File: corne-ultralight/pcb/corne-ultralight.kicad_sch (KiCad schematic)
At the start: 108 parts, among them J2 OLED, J7 OLED, SW1 SW_PUSH, SW10 SW_PUSH, SW11 SW_PUSH, SW12 SW_PUSH, SW13 SW_PUSH, SW14 SW_PUSH, SW15 SW_PUSH, SW16 SW_PUSH, SW17 SW_PUSH, SW18 SW_PUSH, SW19 SW_PUSH, SW2 SW_PUSH, SW20 SW_PUSH, SW21 SW_PUSH, SW22 SW_PUSH, SW23 SW_PUSH, SW24 SW_PUSH, SW25 SW_PUSH, SW26 SW_PUSH, SW27 SW_PUSH, SW28 SW_PUSH, SW29 SW_PUSH, SW3 SW_PUSH, SW30 SW_PUSH, SW31 SW_PUSH, SW32 SW_PUSH, SW33 SW_PUSH, SW34 SW_PUSH, SW35 SW_PUSH, SW36 SW_PUSH, SW37 SW_PUSH, SW38 SW_PUSH, SW39 SW_PUSH, SW4 SW_PUSH, SW40 SW_PUSH, SW41 SW_PUSH, SW42 SW_PUSH, SW5 SW_PUSH, SW6 SW_PUSH, SW7 SW_PUSH, SW8 SW_PUSH, SW9 SW_PUSH, U1 ProMicro, U2 ProMicro

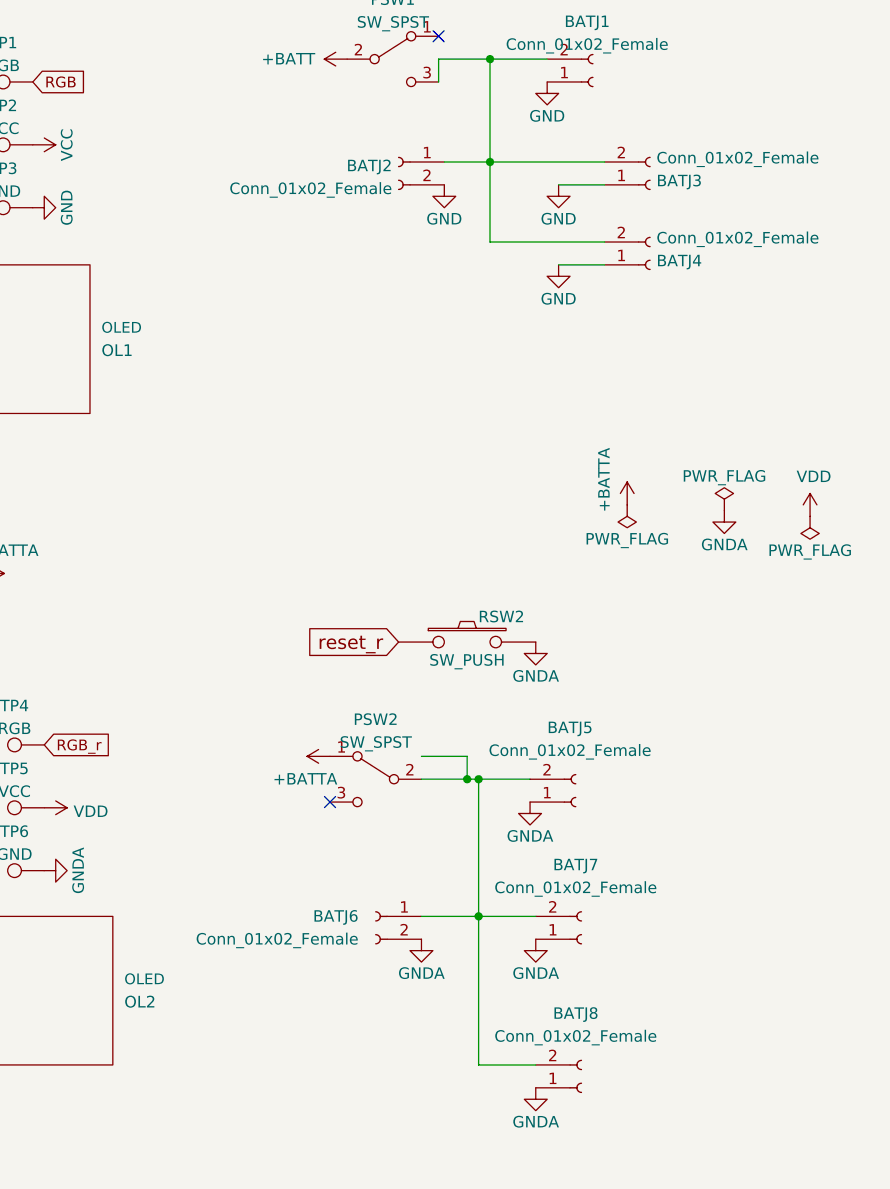
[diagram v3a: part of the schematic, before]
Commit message: Bottom JST connectors aligned
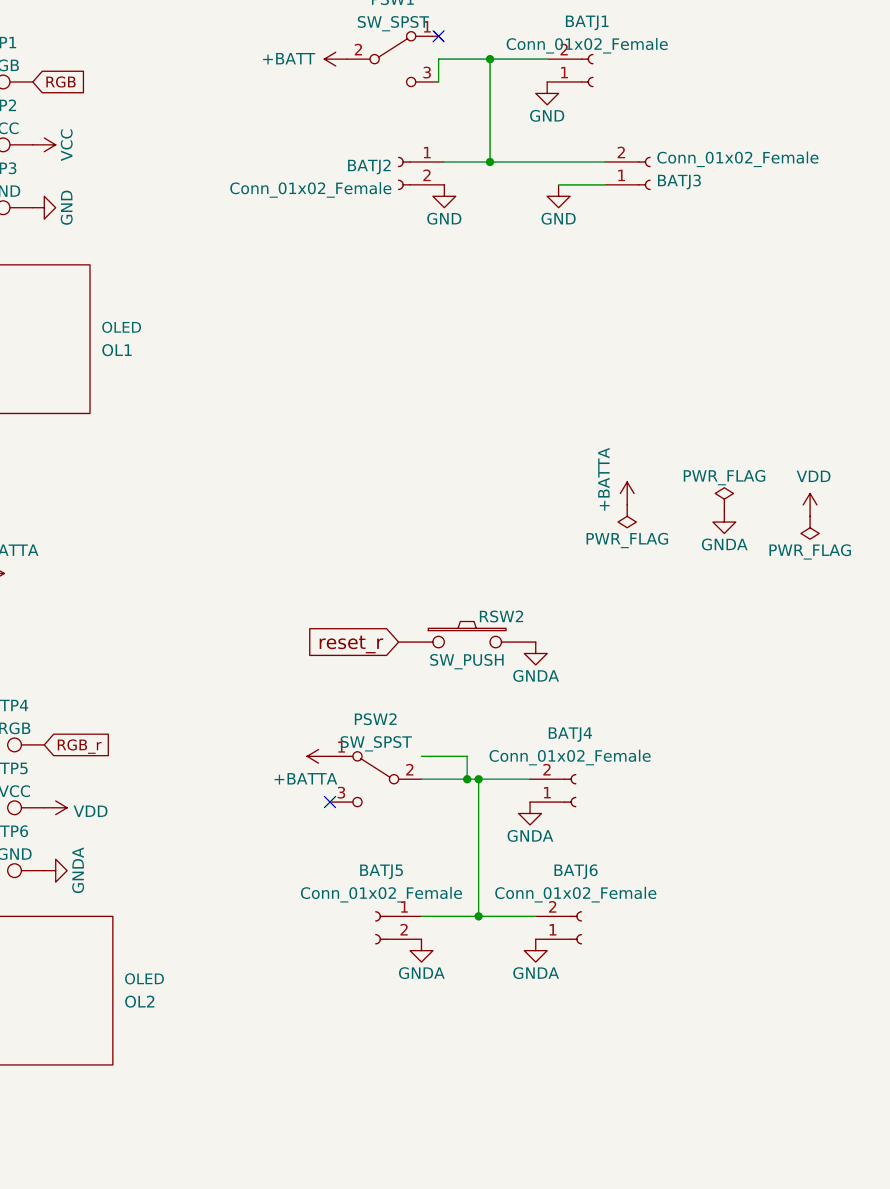
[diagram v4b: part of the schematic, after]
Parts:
- removed BATJ4, BATJ8: Conn_01x02_Female, Connector_JST:JST_PH_S2B-PH-K_1x02_P2.00mm_Horizontal, symbol Connector:Conn_01x02_Female
- renumbered BATJ5 to BATJ4, BATJ6 to BATJ5, BATJ7 to BATJ6

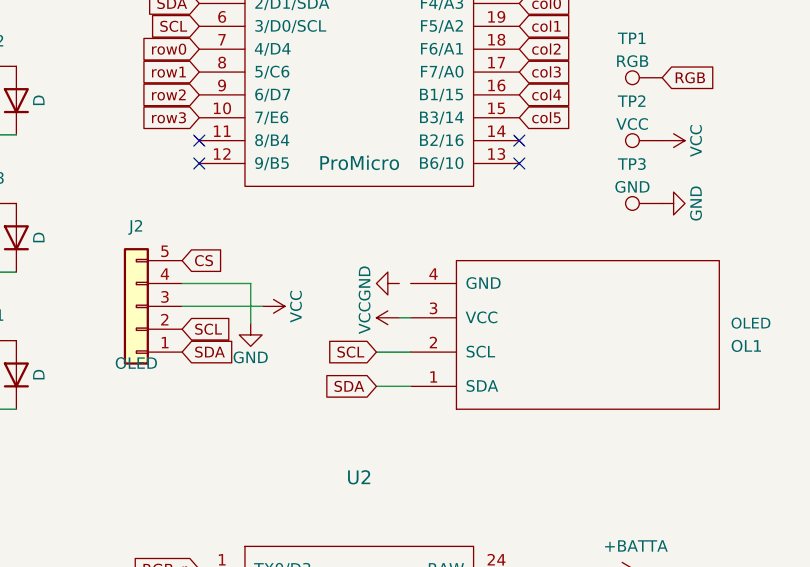
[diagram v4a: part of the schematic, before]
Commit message: All JST connectors routed
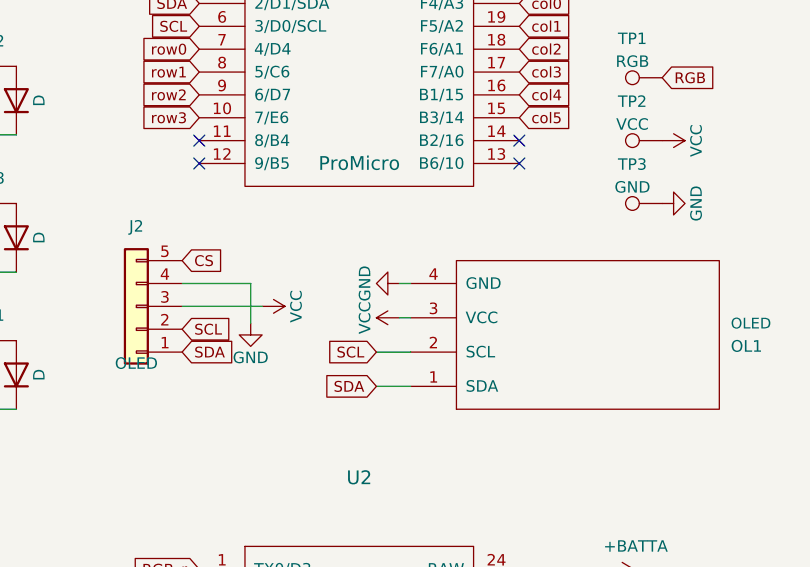
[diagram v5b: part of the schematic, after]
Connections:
- net GND: now also OL1.4 (GND)
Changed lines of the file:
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@@
+	(wire
+		(pts
+			(xy 162.56 63.5) (xy 163.83 63.5)
+		)
+		(stroke
+			(width 0)
+			(type default)
+		)
+	)
 	(wire
 		(pts

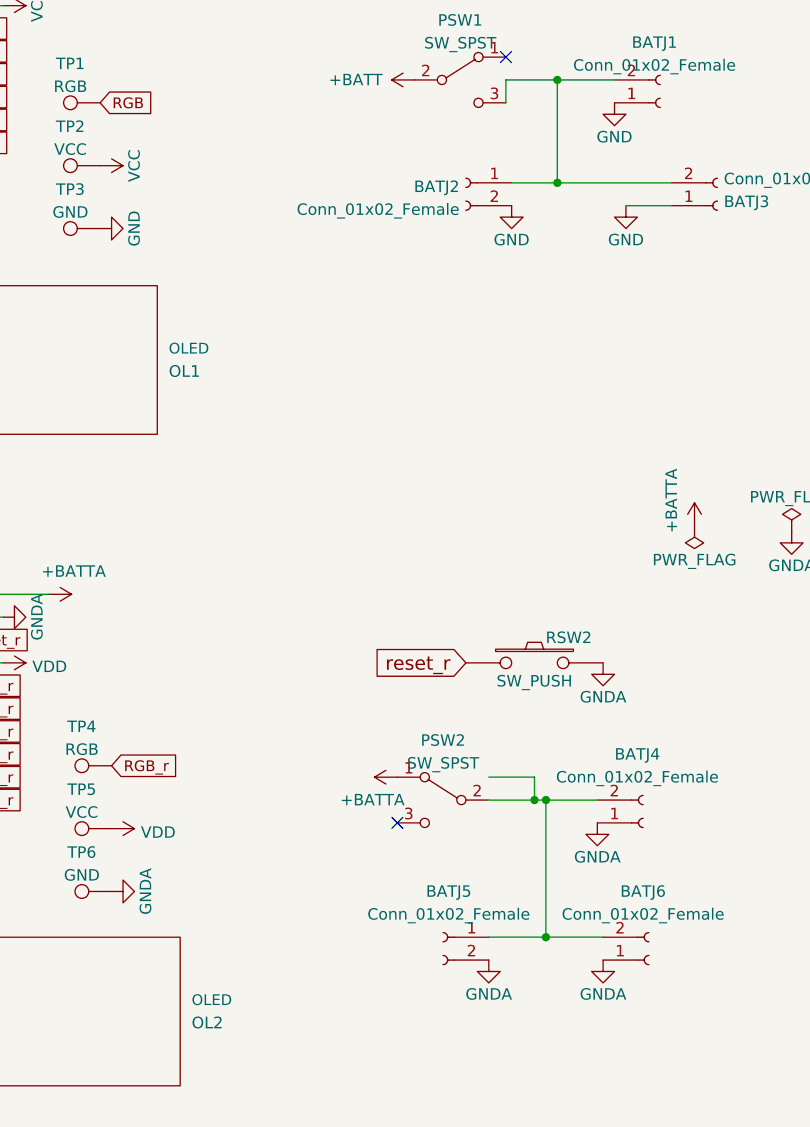
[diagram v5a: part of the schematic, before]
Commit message: BAT pines assignment fixes
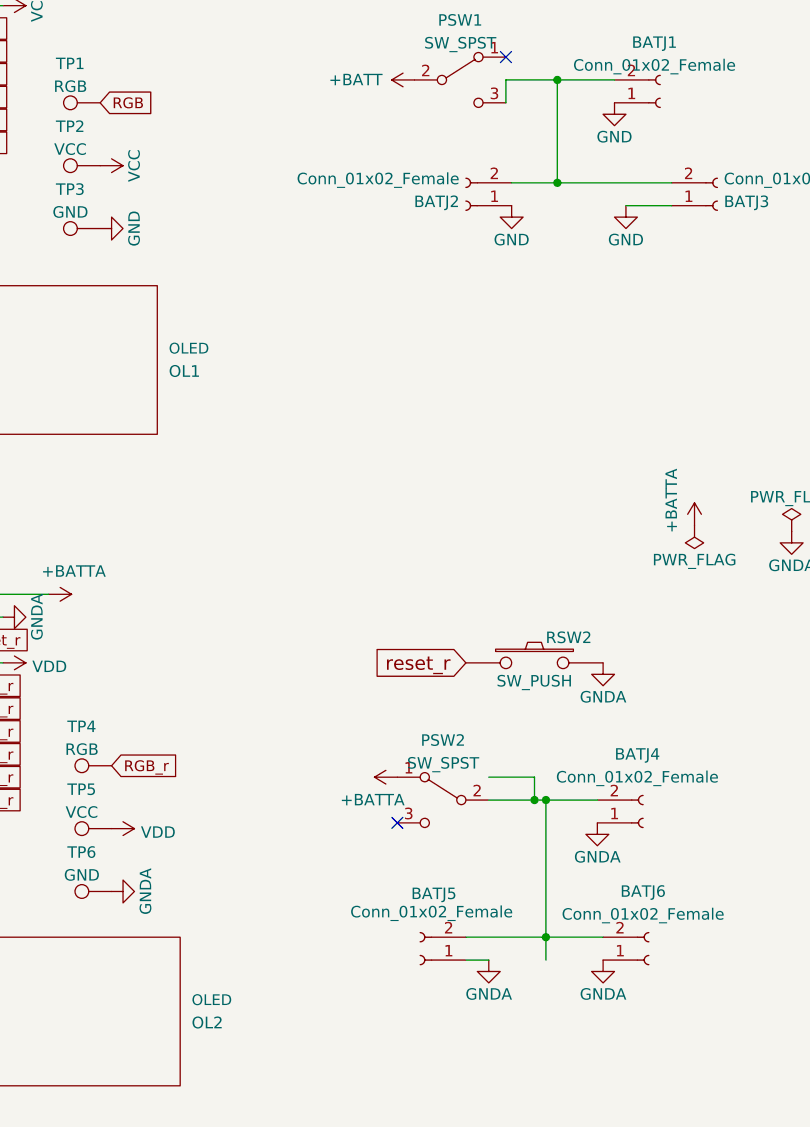
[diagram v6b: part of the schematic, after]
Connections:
- net GND: now also BATJ2.1 (Pin_1); no longer BATJ2.2 (Pin_2)
- net GNDA: now also BATJ5.1 (Pin_1); no longer BATJ5.2 (Pin_2)
- net at BATJ4.2 (Pin_2), BATJ6.2 (Pin_2), PSW2.2 (B): now also BATJ5.2 (Pin_2); no longer BATJ5.1 (Pin_1)
- net at BATJ1.2 (Pin_2), BATJ3.2 (Pin_2), PSW1.3 (C): now also BATJ2.2 (Pin_2); no longer BATJ2.1 (Pin_1)
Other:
- moved on the sheet: BATJ2, BATJ5
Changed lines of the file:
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@@
 	)
 	(junction
+		(at 242.57 49.53)
+		(diameter 0)
+		(color 0 0 0 0)
+	)
+	(junction
 		(at 66.675 46.99)
 		(diameter 0)
@@
 	)
 	(junction
-		(at 242.57 49.53)
-		(diameter 0)
-		(color 0 0 0 0)
-	)
-	(junction
 		(at 48.895 62.23)
 		(diameter 0)
@@
 	(wire
 		(pts
+			(xy 237.49 49.53) (xy 242.57 49.53)
+		)
+		(stroke
+			(width 0)
+			(type default)
+		)
+	)
+	(wire
+		(pts
 			(xy 49.53 129.54) (xy 67.31 129.54)
 		)
@@
 	(wire
 		(pts
+			(xy 241.3 135.89) (xy 241.3 133.35)
+		)
+		(stroke
+			(width 0)
+			(type default)
+		)
+	)
+	(wire
+		(pts
 			(xy 140.335 27.305) (xy 137.795 27.305)
 		)
@@
 	(wire
 		(pts
+			(xy 232.41 135.89) (xy 234.95 135.89)
+		)
+		(stroke
+			(width 0)
+			(type default)
+		)
+	)
+	(wire
+		(pts
 			(xy 85.09 144.78) (xy 102.87 144.78)
 		)
@@
 	(wire
 		(pts
-			(xy 234.95 133.35) (xy 241.3 133.35)
-		)
-		(stroke
-			(width 0)
-			(type default)
-		)
-	)
-	(wire
-		(pts
 			(xy 102.235 77.47) (xy 120.015 77.47)
 		)
@@
 	(wire
 		(pts
-			(xy 237.49 49.53) (xy 242.57 49.53)
-		)
-		(stroke
-			(width 0)
-			(type default)
-		)
-	)
-	(wire
-		(pts
 			(xy 105.41 121.92) (xy 105.41 137.16)
 		)
@@
 	(wire
 		(pts
+			(xy 232.41 133.35) (xy 241.3 133.35)
+		)
+		(stroke
+			(width 0)
+			(type default)
+		)
+	)
+	(wire
+		(pts
 			(xy 86.995 54.61) (xy 86.995 69.85)
 		)
@@
 	(symbol
 		(lib_id "Connector:Conn_01x02_Female")
-		(at 229.87 133.35 0)
-		(mirror y)
+		(at 227.33 135.89 180)
 		(unit 1)
 		(exclude_from_sim no)
@@
 		(on_board yes)
 		(dnp no)
-		(fields_autoplaced yes)
 		(property "Reference" "BATJ5"
-			(at 230.505 128.27 0)
+			(at 228.854 128.524 0)
 			(effects
 				(font
@@
 		)
 		(property "Value" "Conn_01x02_Female"
-			(at 230.505 130.81 0)
+			(at 228.6 130.556 0)
 			(effects
 				(font
@@
 		)
 		(property "Footprint" "Connector_JST:JST_PH_S2B-PH-K_1x02_P2.00mm_Horizontal"
-			(at 229.87 133.35 0)
+			(at 227.33 135.89 0)
 			(effects
 				(font
@@
 		)
 		(property "Datasheet" "~"
-			(at 229.87 133.35 0)
+			(at 227.33 135.89 0)
 			(effects
 				(font
@@
 		)
 		(property "Description" ""
-			(at 229.87 133.35 0)
+			(at 227.33 135.89 0)
 			(effects
 				(font
@@
 	(symbol
 		(lib_id "Connector:Conn_01x02_Female")
-		(at 232.41 49.53 0)
-		(mirror y)
+		(at 232.41 52.07 180)
 		(unit 1)
 		(exclude_from_sim no)
@@
 		(on_board yes)
 		(dnp no)
-		(fields_autoplaced yes)
 		(property "Reference" "BATJ2"
-			(at 231.6988 49.9653 0)
+			(at 231.6988 51.6347 0)
 			(effects
 				(font
@@
 		)
 		(property "Value" "Conn_01x02_Female"
-			(at 231.6988 52.5022 0)
+			(at 231.6988 49.0978 0)
 			(effects
 				(font
@@
 		)
 		(property "Footprint" "Connector_JST:JST_PH_S2B-PH-K_1x02_P2.00mm_Horizontal"
-			(at 232.41 49.53 0)
+			(at 232.41 52.07 0)
 			(effects
 				(font
@@
 		)
 		(property "Datasheet" "~"
-			(at 232.41 49.53 0)
+			(at 232.41 52.07 0)
 			(effects
 				(font
@@
 		)
 		(property "Description" ""
-			(at 232.41 49.53 0)
+			(at 232.41 52.07 0)
 			(effects
 				(font

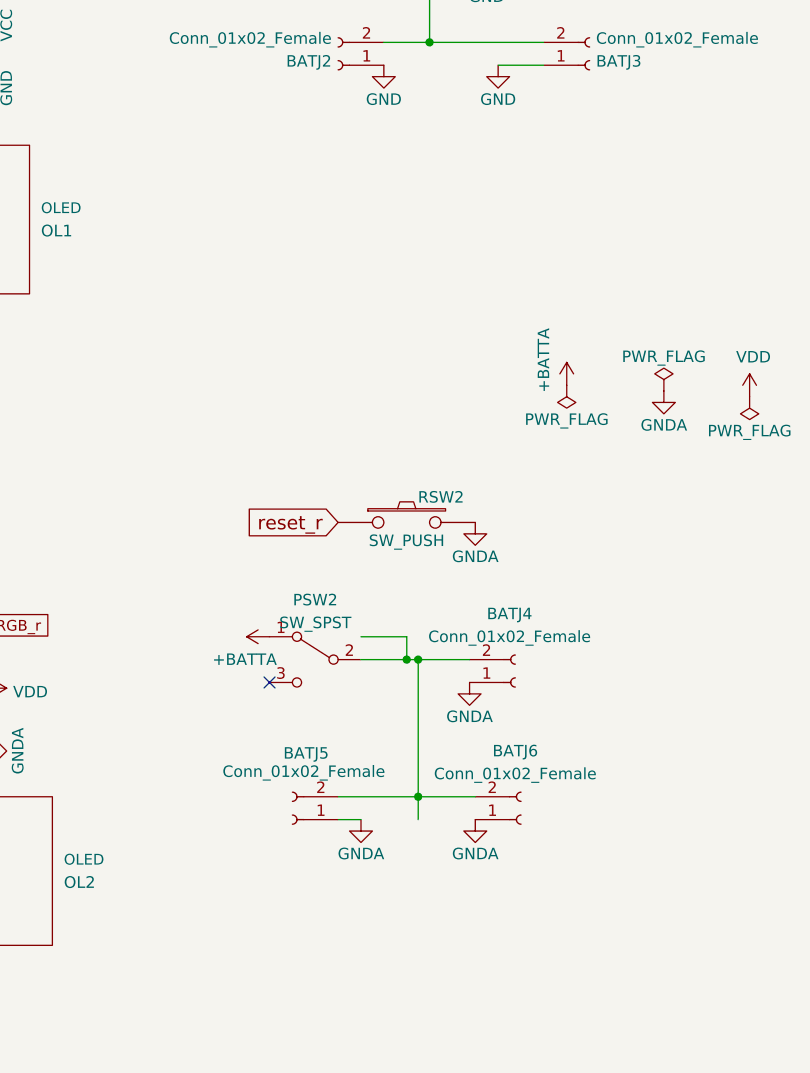
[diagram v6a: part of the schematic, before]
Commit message: Versa mods to support wired builds
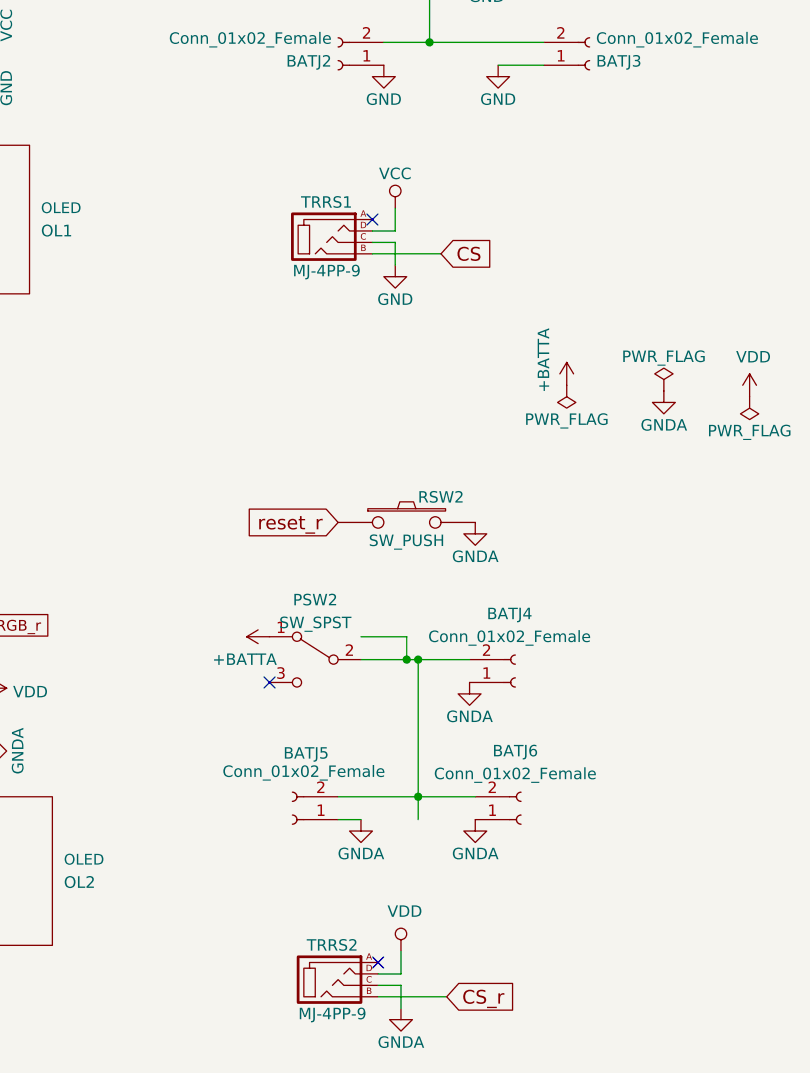
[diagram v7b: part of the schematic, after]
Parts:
- added TRRS1, TRRS2: MJ-4PP-9, kbd:MJ-4PP-9_1side, symbol corne-light-rescue:MJ-4PP-9-kbd
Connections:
- net CS: now also TRRS1.B
- net CS_r: now also TRRS2.B
- net GND: now also TRRS1.C
- net GNDA: now also TRRS2.C
- net VCC: now also TRRS1.D
- net VDD: now also TRRS2.D
- no-connect marks 10 -> 12

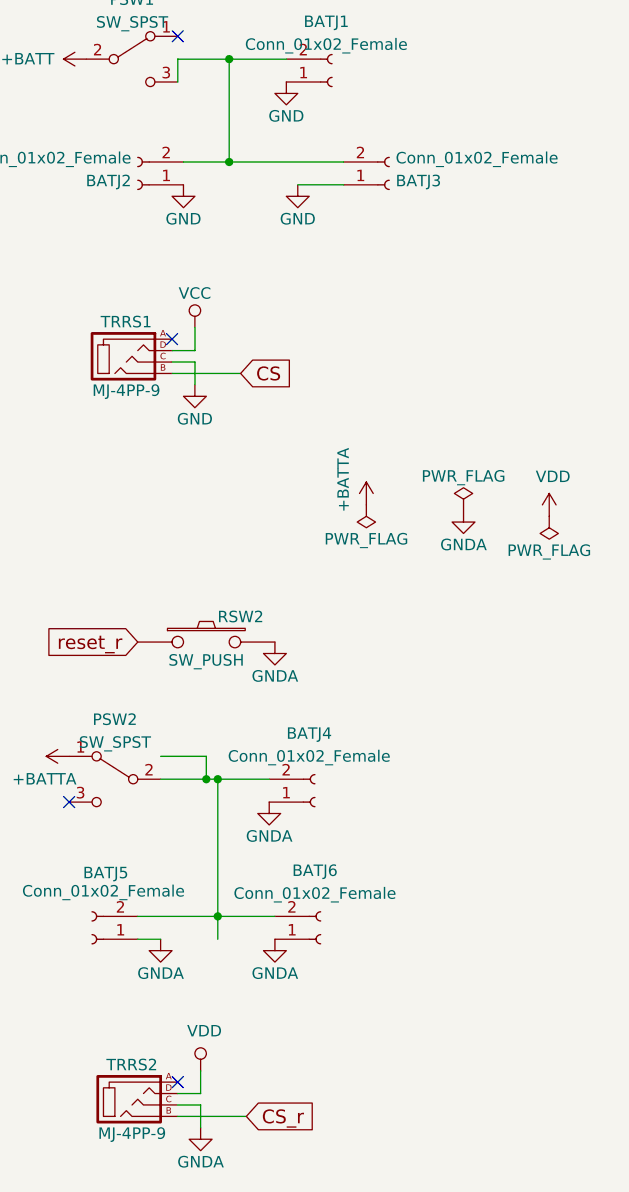
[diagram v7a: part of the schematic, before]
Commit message: Additional JST
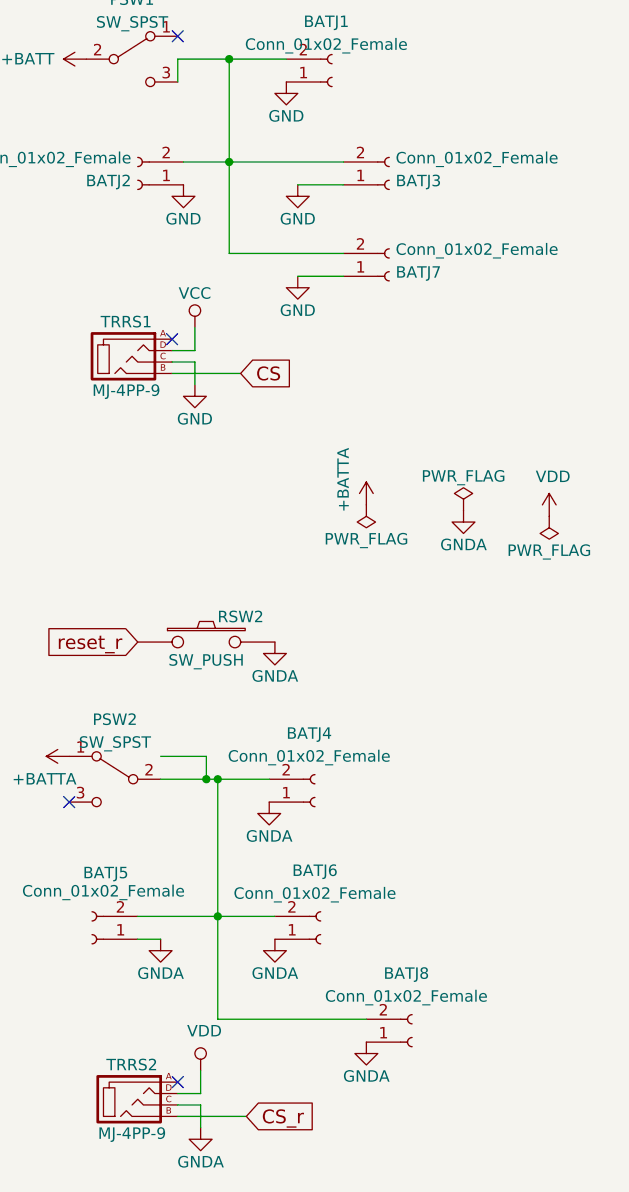
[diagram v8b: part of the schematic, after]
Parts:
- added BATJ7, BATJ8: Conn_01x02_Female, Connector_JST:JST_PH_S2B-PH-K_1x02_P2.00mm_Horizontal, symbol Connector:Conn_01x02_Female
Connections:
- net GND: now also BATJ7.1 (Pin_1)
- net GNDA: now also BATJ8.1 (Pin_1)
- net at BATJ4.2 (Pin_2), BATJ5.2 (Pin_2), BATJ6.2 (Pin_2)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: now also BATJ8.2 (Pin_2)
- net at BATJ1.2 (Pin_2), BATJ2.2 (Pin_2), BATJ3.2 (Pin_2)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: now also BATJ7.2 (Pin_2)
